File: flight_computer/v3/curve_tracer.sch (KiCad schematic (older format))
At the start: 68 parts, among them U1 OPA2387, U10 OPA2387, U10 TLV7031DBV, U11 INA190A4IDDFR, U12 INA190A4IDDFR, U13 INA190A4IDDFR, U14 INA190A4IDDFR, U2 OPA2387, U9 SN74CBT3253

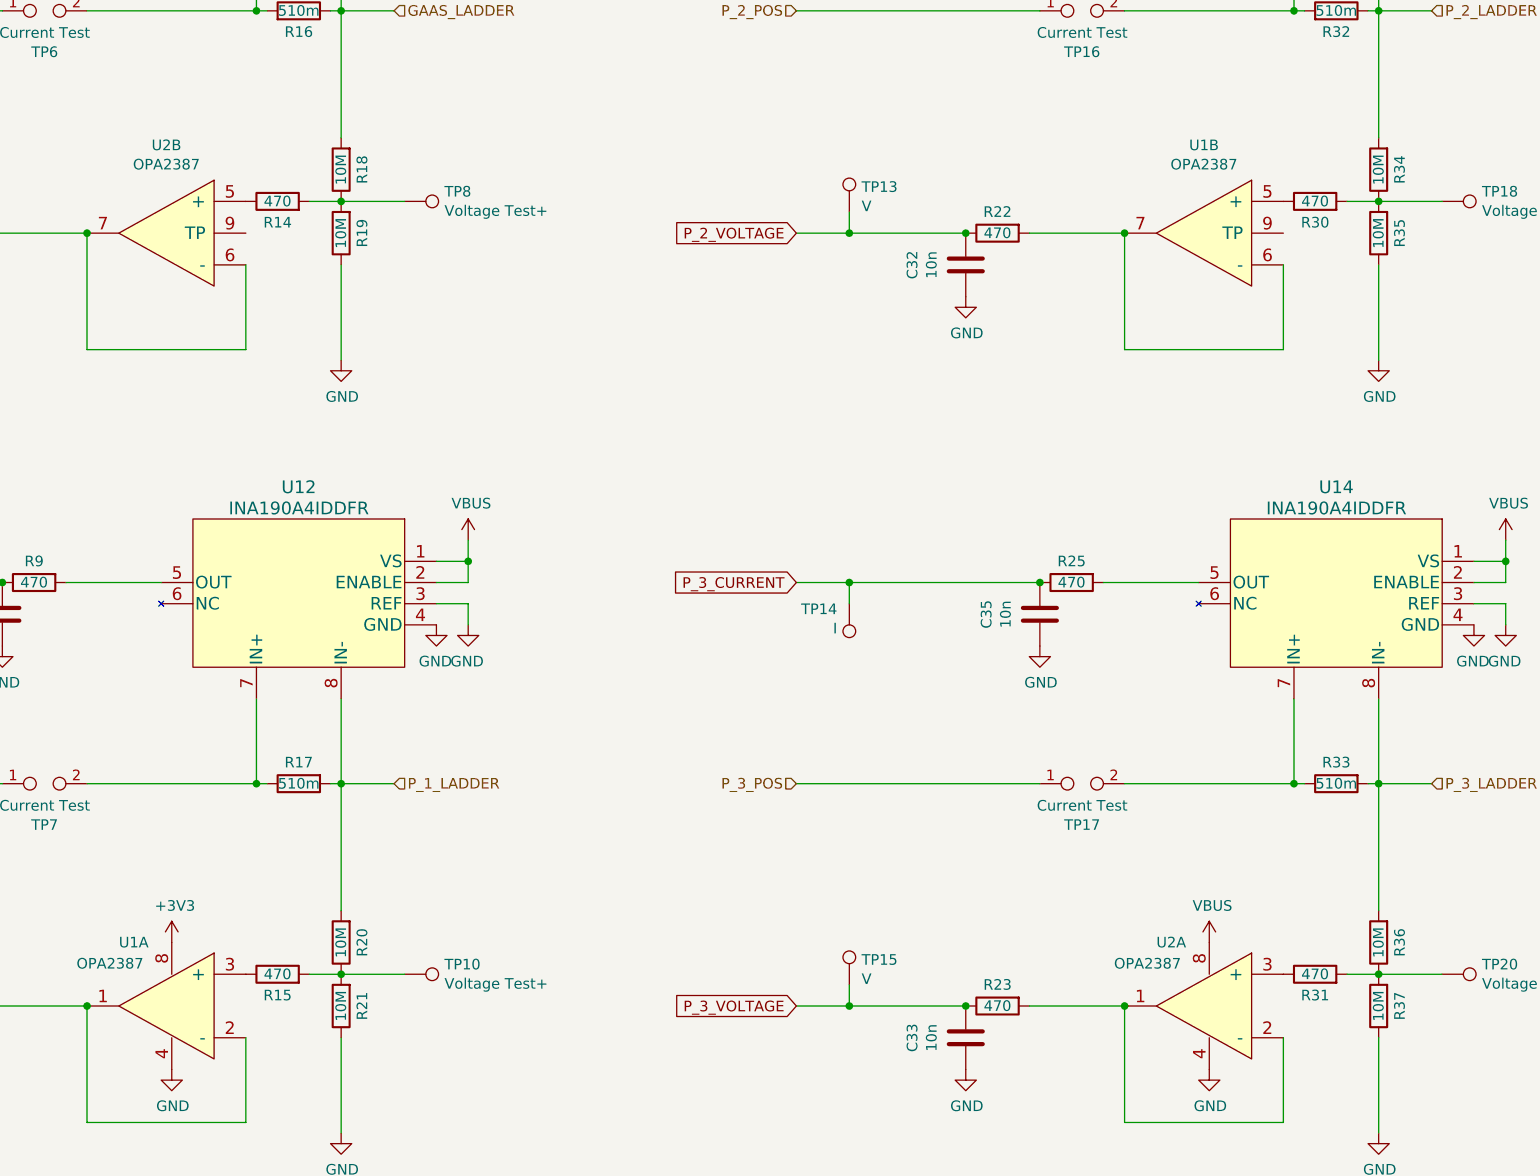
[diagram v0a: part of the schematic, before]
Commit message: Updating based on harnesses
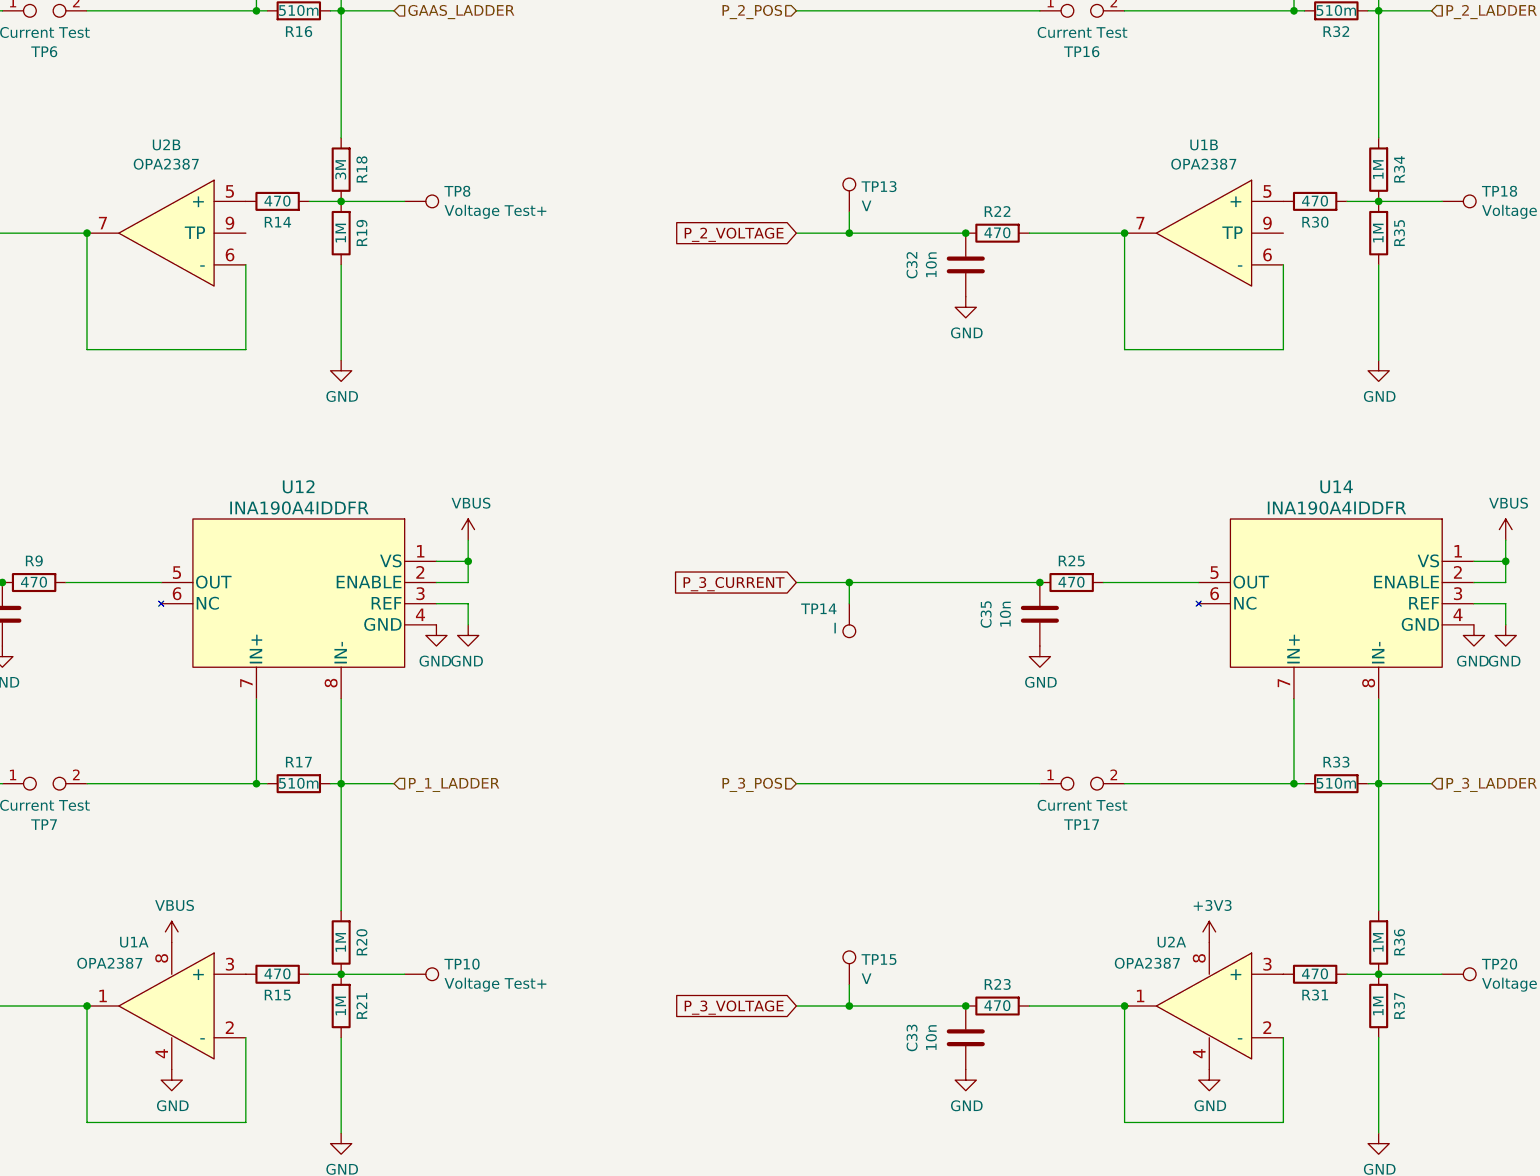
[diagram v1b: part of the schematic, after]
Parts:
- R20, R21, R27, R34, R35, R36, R37: value 10M -> 1M
- R26: value 10M -> 3M
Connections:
- net +3V3: now also U2.8; no longer U10.8
- net VBUS: now also U10.8; no longer U2.8
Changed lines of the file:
@@
 AR Path="/64D8220D/6374DE94" Ref="R19"  Part="1"
 F 0 "R19" V 8200 4700 50  0000 C CNN
-F 1 "10M" V 8300 4700 50  0000 C CNN
+F 1 "1M" V 8300 4700 50  0000 C CNN
 F 2 "Resistor_SMD:R_0603_1608Metric" V 8230 4700 50  0001 C CNN
 F 3 "~" H 8300 4700 50  0001 C CNN
@@
 AR Path="/64D8220D/6374D1E3" Ref="R18"  Part="1"
 F 0 "R18" V 8200 4400 50  0000 C CNN
-F 1 "10M" V 8300 4400 50  0000 C CNN
+F 1 "3M" V 8300 4400 50  0000 C CNN
 F 2 "Resistor_SMD:R_0603_1608Metric" V 8230 4400 50  0001 C CNN
 F 3 "~" H 8300 4400 50  0001 C CNN
@@
 L power:+3V3 #PWR067
 U 1 1 65AE8B55
-P 7500 8050
-F 0 "#PWR067" H 7500 7900 50  0001 C CNN
-F 1 "+3V3" H 7515 8223 50  0000 C CNN
-F 2 "" H 7500 8050 50  0001 C CNN
-F 3 "" H 7500 8050 50  0001 C CNN
-	1    7500 8050
+P 12400 8050
+F 0 "#PWR067" H 12400 7900 50  0001 C CNN
+F 1 "+3V3" H 12415 8223 50  0000 C CNN
+F 2 "" H 12400 8050 50  0001 C CNN
+F 3 "" H 12400 8050 50  0001 C CNN
+	1    12400 8050
 	1    0    0    -1
 $EndComp
@@
 AR Path="/64D8220D/65C6DB54" Ref="R21"  Part="1"
 F 0 "R21" V 8200 8350 50  0000 C CNN
-F 1 "10M" V 8300 8350 50  0000 C CNN
+F 1 "1M" V 8300 8350 50  0000 C CNN
 F 2 "Resistor_SMD:R_0603_1608Metric" V 8230 8350 50  0001 C CNN
 F 3 "~" H 8300 8350 50  0001 C CNN
@@
 AR Path="/64D8220D/65C6DB5A" Ref="R20"  Part="1"
 F 0 "R20" V 8200 8050 50  0000 C CNN
-F 1 "10M" V 8300 8050 50  0000 C CNN
+F 1 "1M" V 8300 8050 50  0000 C CNN
 F 2 "Resistor_SMD:R_0603_1608Metric" V 8230 8050 50  0001 C CNN
 F 3 "~" H 8300 8050 50  0001 C CNN
@@
 AR Path="/64D8220D/65C7B45F" Ref="R35"  Part="1"
 F 0 "R35" V 13100 4700 50  0000 C CNN
-F 1 "10M" V 13200 4700 50  0000 C CNN
+F 1 "1M" V 13200 4700 50  0000 C CNN
 F 2 "Resistor_SMD:R_0603_1608Metric" V 13130 4700 50  0001 C CNN
 F 3 "~" H 13200 4700 50  0001 C CNN
@@
 AR Path="/64D8220D/65C7B465" Ref="R34"  Part="1"
 F 0 "R34" V 13100 4400 50  0000 C CNN
-F 1 "10M" V 13200 4400 50  0000 C CNN
+F 1 "1M" V 13200 4400 50  0000 C CNN
 F 2 "Resistor_SMD:R_0603_1608Metric" V 13130 4400 50  0001 C CNN
 F 3 "~" H 13200 4400 50  0001 C CNN
@@
 AR Path="/64D8220D/65C84B21" Ref="R37"  Part="1"
 F 0 "R37" V 13100 8350 50  0000 C CNN
-F 1 "10M" V 13200 8350 50  0000 C CNN
+F 1 "1M" V 13200 8350 50  0000 C CNN
 F 2 "Resistor_SMD:R_0603_1608Metric" V 13130 8350 50  0001 C CNN
 F 3 "~" H 13200 8350 50  0001 C CNN
@@
 AR Path="/64D8220D/65C84B27" Ref="R36"  Part="1"
 F 0 "R36" V 13100 8050 50  0000 C CNN
-F 1 "10M" V 13200 8050 50  0000 C CNN
+F 1 "1M" V 13200 8050 50  0000 C CNN
 F 2 "Resistor_SMD:R_0603_1608Metric" V 13130 8050 50  0001 C CNN
 F 3 "~" H 13200 8050 50  0001 C CNN
@@
 L power:VBUS #PWR086
 U 1 1 65C89D4A
-P 12400 8050
-F 0 "#PWR086" H 12400 7900 50  0001 C CNN
-F 1 "VBUS" H 12415 8223 50  0000 C CNN
-F 2 "" H 12400 8050 50  0001 C CNN
-F 3 "" H 12400 8050 50  0001 C CNN
-	1    12400 8050
-	1    0    0    -1
-$EndComp
+P 7500 8050
+F 0 "#PWR086" H 7500 7900 50  0001 C CNN
+F 1 "VBUS" H 7515 8223 50  0000 C CNN
+F 2 "" H 7500 8050 50  0001 C CNN
+F 3 "" H 7500 8050 50  0001 C CNN
+	1    7500 8050
+	1    0    0    -1
+$EndComp
